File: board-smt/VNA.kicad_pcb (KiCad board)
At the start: 2 copper layers, 100 x 85 mm, 167 parts, among them J1 Conn_02x07_Odd_Even, J11 Conn_01x01, J13 Barrel_Jack, J14 Conn_01x01, J15 Conn_01x02, J16 Conn_01x01, J18 Conn_01x01, J19 Conn_01x01, J2 Conn_Coaxial, J20 Conn_01x01, J21 Conn_01x01, J24 USB_B, J3 Conn_01x01, J4 Conn_01x01, J5 Conn_01x01, J6 Conn_01x01, J7 Conn_01x01, J8 Conn_01x01, J9 Conn_Coaxial, Q3 S9018, SW1 SW_DPDT_x2, U1 SI5351A, U10 MT3608, U11 CN3052, U12 SI5351A, U2 LM339, U3 SA612, U4 SA612, U5 SA612, U6 LM358, U7 LM358, U8 AMS1117-3V3, U9 78M05_TO252, Y1 27 MHz

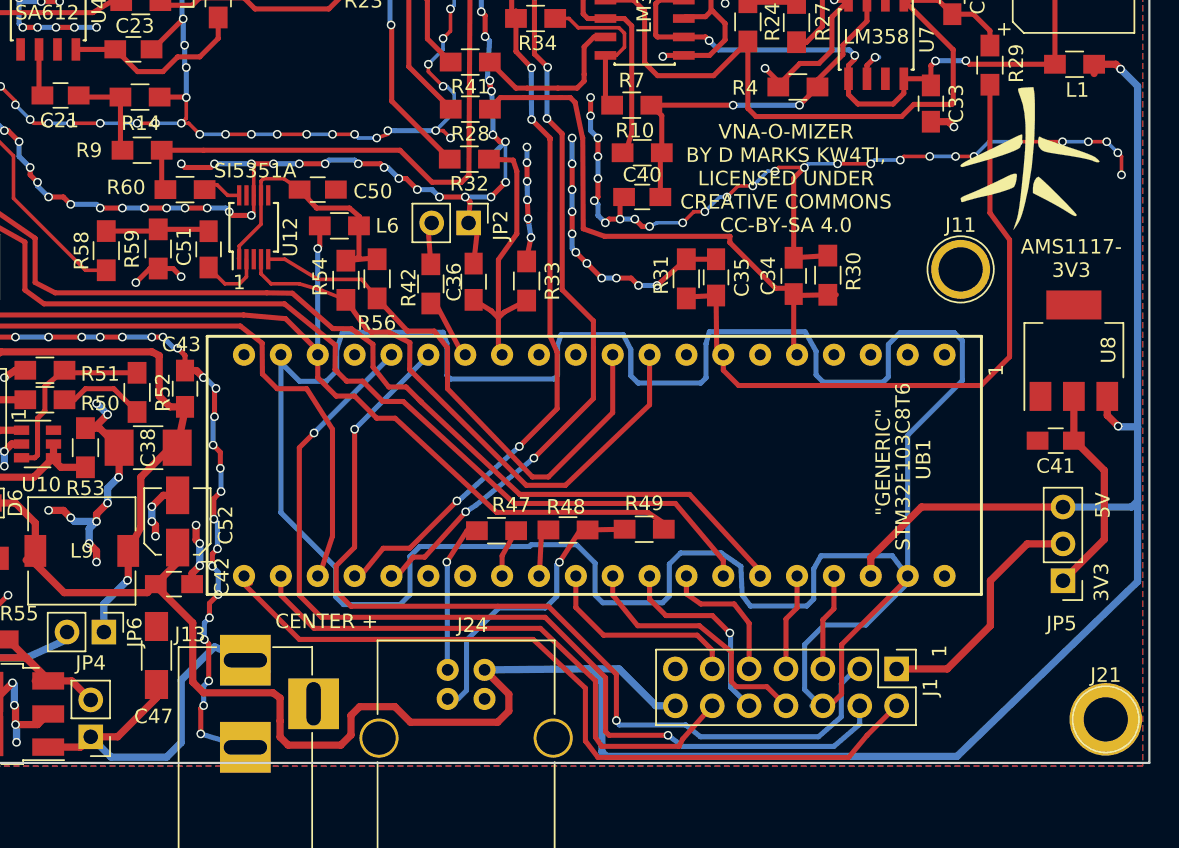
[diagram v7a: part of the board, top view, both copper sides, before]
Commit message: Put USB back through filter again
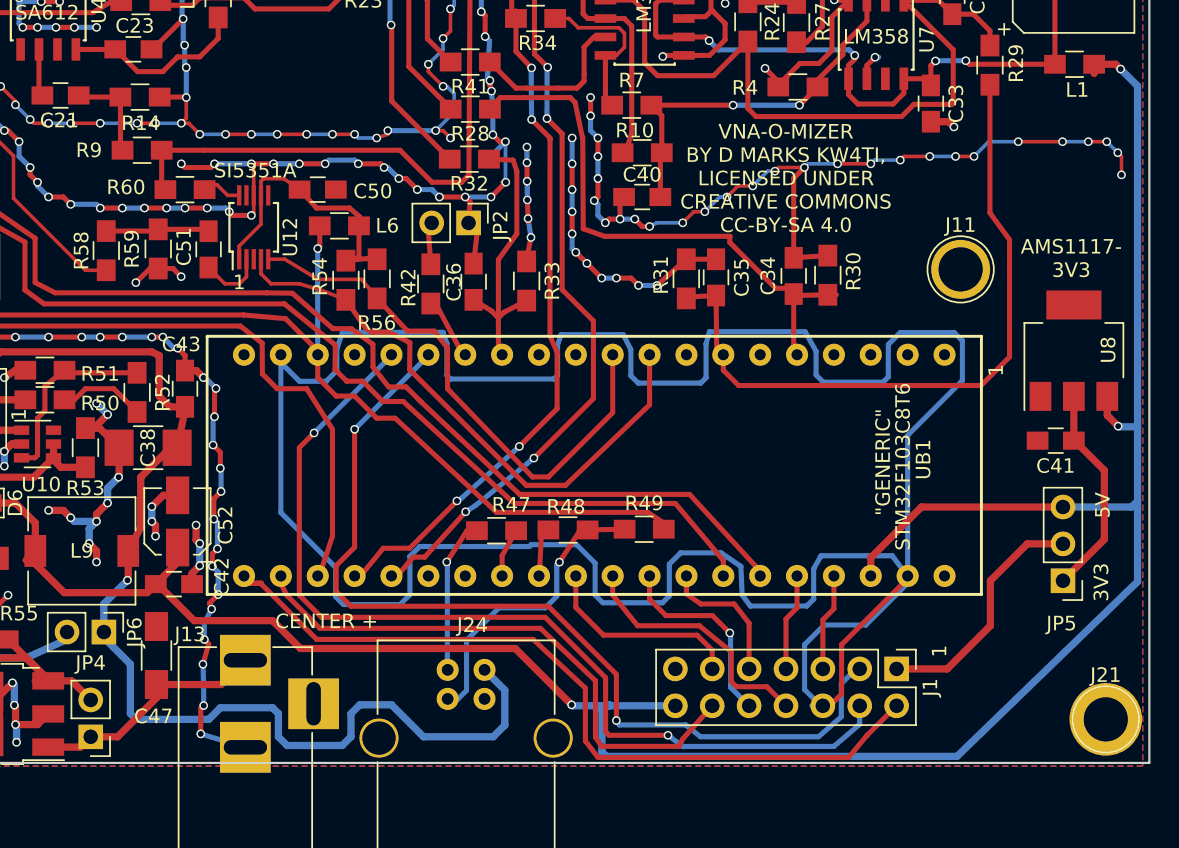
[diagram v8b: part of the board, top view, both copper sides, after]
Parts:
- removed G***: LOGO, VNA:VNAOMizer
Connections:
- J24 pad 1: +5V -> POWFILT
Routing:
- net POWFILT: track 40.9 -> 84.1 mm
- net +5V: track 185.2 -> 167.9 mm, vias 2 -> 3
- net Net-(C47-Pad1): track 31.8 -> 18.3 mm
